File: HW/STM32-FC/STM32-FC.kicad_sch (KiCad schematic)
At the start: 39 parts, among them J1 GH 1.25mm 6P, Q1 S9013, SW2 SW_DIP_x03, U1 STM32F407VETx, Y1 16MHz

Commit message: Test software v1
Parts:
- renumbered C9 to C10, C10 to C11, C11 to C12, C12 to C13, C35 to C5, C5 to C6, C6 to C7, C7 to C8, C8 to C9, R3 to R1, R1 to R2, R2 to R3, SW2 to SW1

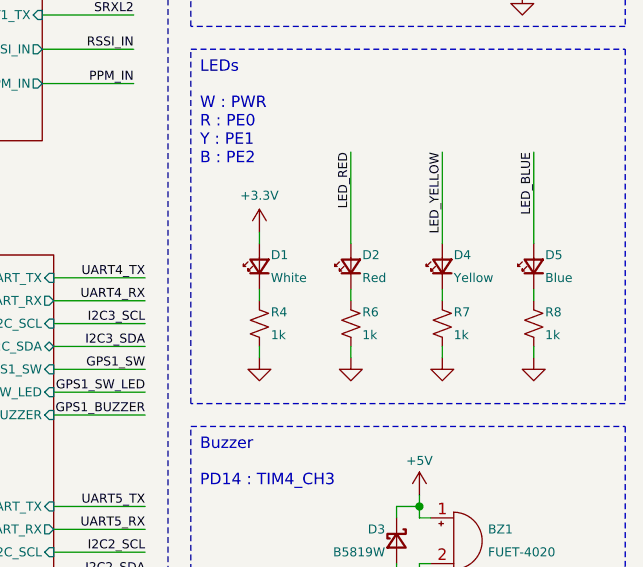
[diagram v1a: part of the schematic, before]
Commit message: SRXL2_readByte() array index out bug fix
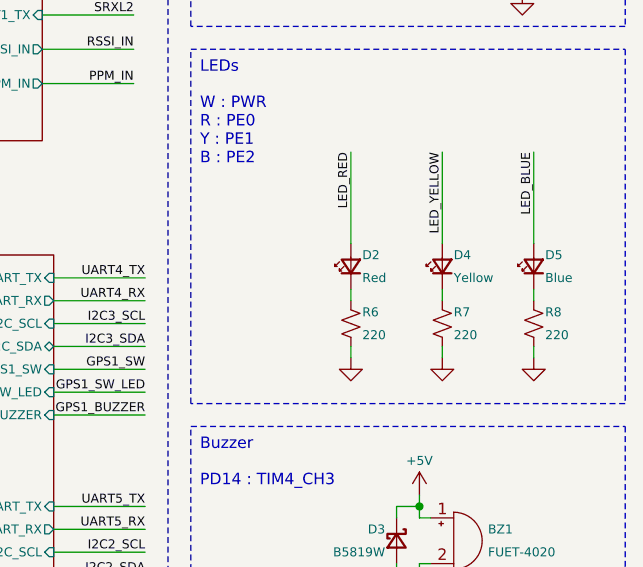
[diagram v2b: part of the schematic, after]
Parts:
- removed D1: White, LED_SMD:LED_0402_1005Metric, symbol Device:LED_Small
- removed R4: 1k, Resistor_SMD:R_0402_1005Metric, symbol Device:R_Small_US
- R6, R7, R8: value 1k -> 220

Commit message: Log add. backup
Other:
- sheet Sensors ports: added GYRO1_INT, GYRO2_INT; removed none
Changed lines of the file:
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@@
 	(wire
 		(pts
-			(xy 139.7 121.92) (xy 149.86 121.92)
+			(xy 139.7 127) (xy 149.86 127)
 		)
 		(stroke
@@
 	(wire
 		(pts
+			(xy 139.7 121.92) (xy 149.86 121.92)
+		)
+		(stroke
+			(width 0)
+			(type default)
+		)
+	)
+	(wire
+		(pts
 			(xy 109.22 60.96) (xy 119.38 60.96)
 		)
@@
 	(wire
 		(pts
+			(xy 139.7 124.46) (xy 149.86 124.46)
+		)
+		(stroke
+			(width 0)
+			(type default)
+		)
+	)
+	(wire
+		(pts
 			(xy 83.82 41.91) (xy 81.28 41.91)
 		)
@@
 		)
 	)
+	(label "GYRO1_INT"
+		(at 149.86 121.92 180)
+		(effects
+			(font
+				(size 1 1)
+			)
+			(justify right bottom)
+		)
+	)
 	(label "PM_CURRENT"
 		(at 149.86 29.21 180)
@@
 		)
 	)
+	(label "GYRO2_INT"
+		(at 149.86 124.46 180)
+		(effects
+			(font
+				(size 1 1)
+			)
+			(justify right bottom)
+		)
+	)
 	(label "FLASH_NSS"
 		(at 149.86 63.5 180)
@@
 	)
 	(label "BARO_INT"
-		(at 149.86 121.92 180)
+		(at 149.86 127 180)
 		(effects
 			(font
@@
 		)
 		(pin "BARO_INT" output
+			(at 139.7 127 0)
+			(effects
+				(font
+					(size 1 1)
+				)
+				(justify right)
+			)
+		)
+		(pin "GYRO2_INT" output
+			(at 139.7 124.46 0)
+			(effects
+				(font
+					(size 1 1)
+				)
+				(justify right)
+			)
+		)
+		(pin "GYRO1_INT" output
 			(at 139.7 121.92 0)
 			(effects
